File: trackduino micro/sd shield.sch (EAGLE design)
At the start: 12 parts, among them U1 FT232RL-BASICSSOP

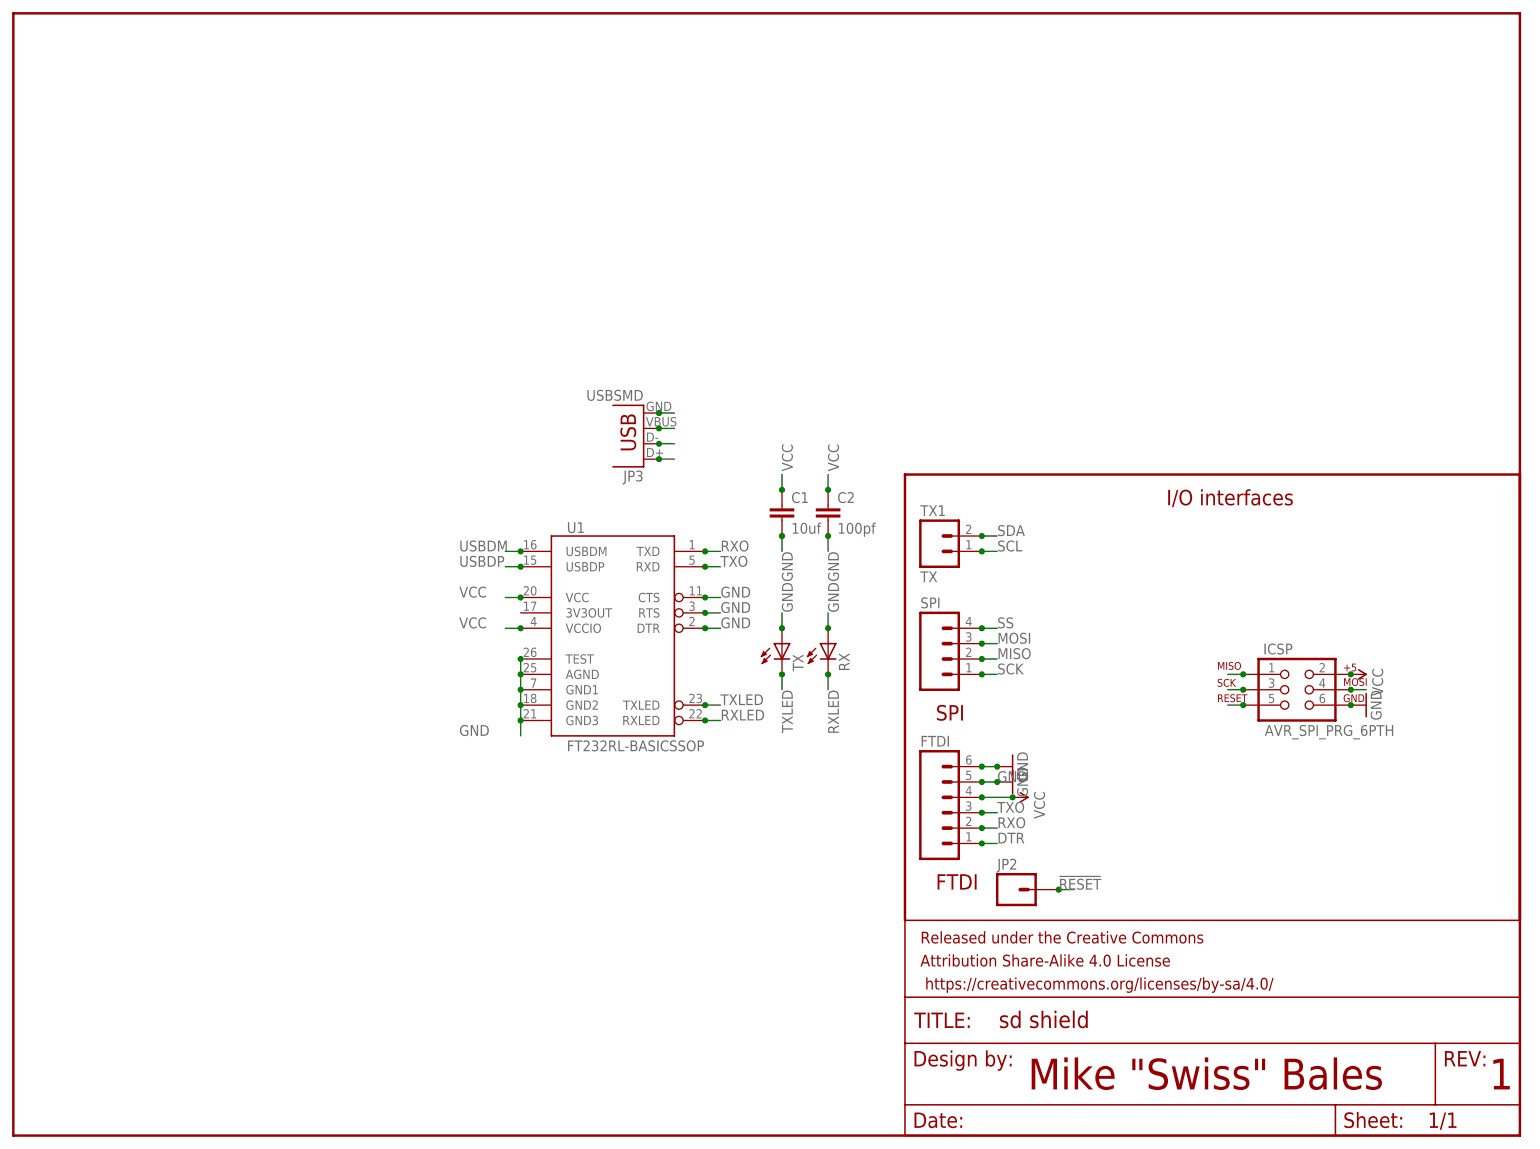
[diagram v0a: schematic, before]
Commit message: Shield Updates
added sd storage shield, added fetid chip to programming shield. Moved
test boards to correct folder.
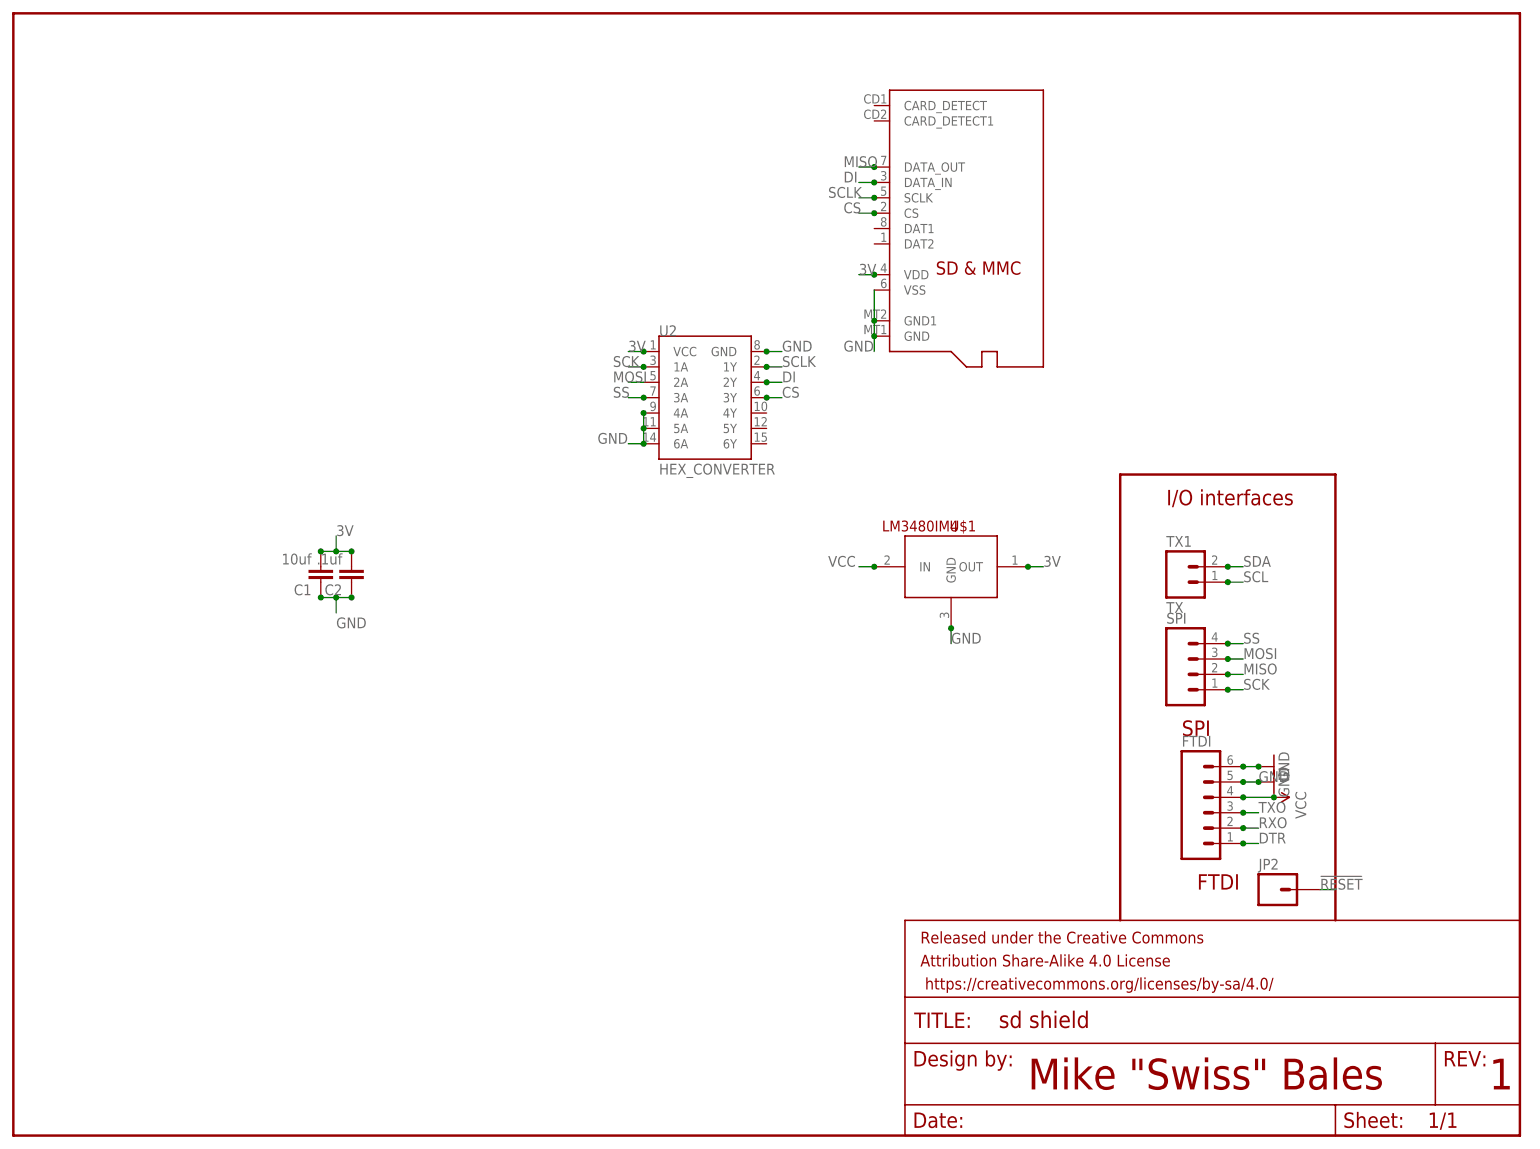
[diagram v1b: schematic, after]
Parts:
- removed ICSP: AVR_SPI_PRG_6PTH, SparkFun-Connectors:AVR_SPI_PRG_6PTH
- removed JP3: USBSMD, SparkFun-Connectors:USBSMD
- removed RX, TX: (no value), adafruit:LEDCHIP-LED0805
- removed U1: FT232RL-BASICSSOP, SparkFun-DigitalIC:FT232RL-BASICSSOP
- added U$1: LM3480IM4, SparkFun-PowerIC:LM3480IM4
- added U$2: MICROSD, adafruit:MICROSD
- added U2: HEX_CONVERTER, SparkFun-DigitalIC:HEX_CONVERTER
- C2: value 100pf -> .1uf
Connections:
- removed net RXLED: RX.C, U1.RXLED
- removed net TXLED: TX.C, U1.TXLED
- removed net USBDM: JP3.D-, U1.USBDM
- removed net USBDP: JP3.D+, U1.USBDP
- new net 3V: C1.2, C2.2, U$1.OUT, U$2.VDD, U2.VCC
- new net CS: U$2.CS, U2.3Y
- new net DI: U$2.DATA_IN, U2.2Y
- new net SCLK: U$2.SCLK, U2.1Y
- net !RESET: no longer ICSP.5
- net GND: now also C1.1, C2.1, U$1.GND, U$2.GND, U$2.GND1, U$2.VSS, U2.4A, U2.5A, U2.6A, U2.GND; no longer C1.2, C2.2, ICSP.6, JP3.GND, RX.A, TX.A, U1.AGND, U1.CTS, U1.DTR, U1.GND1, U1.GND2, U1.GND3, U1.RTS, U1.TEST
- net MISO: now also U$2.DATA_OUT; no longer ICSP.1
- net MOSI: now also U2.2A; no longer ICSP.4
- net RXO: no longer U1.TXD
- net SCK: now also U2.1A; no longer ICSP.3
- net SS: now also U2.3A
- net TXO: no longer U1.RXD
- net VCC: now also U$1.IN; no longer C1.1, C2.1, ICSP.2, JP3.VBUS, U1.VCC, U1.VCCIO
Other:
- moved on the sheet: C1, C2, FTDI, JP2, SPI, TX1
